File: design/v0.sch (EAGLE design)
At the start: 3 parts

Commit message: Update schematic
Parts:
- removed R1: 9.76k, rcl:R-EU_0207/10
- added D1, D2, D3, D4, D5, D6, D7, D8, D9: 1N4004, diode:1N4004
- added U$10, U$3, U$4, U$5, U$6, U$7, U$8, U$9: CHERRY-MX, cherrymx:CHERRY-MX
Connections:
- new net N$10: D1.C, D4.C, D7.C, U$1.24
- new net N$11: D2.C, D5.C, D8.C, U$1.22
- new net N$12: D3.C, D6.C, D9.C, U$1.21
- new net N$13: U$1.27, U$2.PIN-1, U$3.PIN-1, U$4.PIN-1
- new net N$14: U$1.26, U$5.PIN-1, U$6.PIN-1, U$7.PIN-1
- new net N$15: U$1.25, U$10.PIN-1, U$8.PIN-1, U$9.PIN-1
- new net N$3: D3.A, U$4.PIN-2
- new net N$5: D5.A, U$6.PIN-2
- new net N$6: D6.A, U$7.PIN-2
- new net N$7: D9.A, U$10.PIN-2
- new net N$8: D8.A, U$9.PIN-2
- new net N$9: D7.A, U$8.PIN-2
- net N$1: now also D1.A, U$2.PIN-2; no longer U$1.38, U$2.PIN-1
- net N$2: now also D2.A, U$3.PIN-2; no longer R1.2, U$1.36, U$2.PIN-2
- net N$4: now also D4.A, U$5.PIN-2; no longer R1.1, U$1.17
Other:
- moved on the sheet: U$2

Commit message: Update schematic
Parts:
- removed U$10, U$2, U$3, U$4, U$5, U$6, U$7, U$8, U$9: CHERRY-MX, cherrymx:CHERRY-MX
- added LED1, LED2, LED3: TLLG4400, led:TLLG4400
- added R1, R2: 9.76k, rcl:R-EU_VMTA55
- added R3, R4, R5: 60, rcl:R-EU_VMTA55
- added S1: RESET, switch-omron:10-XX
- added S2, S3: (no value), switch-omron:10-XX
- added U1, U2, U3, U4, U5, U6, U7, U8, U9: CHERRY-MX, cherrymx:CHERRY-MX
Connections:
- removed net N$15 (its old number): U$1.25, U$10.PIN-1, U$8.PIN-1, U$9.PIN-1
- removed net N$8: D8.A, U$9.PIN-2
- new net N$10: R1.1, R2.1, S2.S, S3.S, U$1.36
- new net N$11: R2.2, U$1.9
- new net N$12: S2.P, S3.P, U$1.8
- new net N$18: D6.A, U6.PIN-2
- new net N$19: D3.A, U3.PIN-2
- new net N$20: D9.A, U9.PIN-2
- new net N$21: D8.A, U8.PIN-2
- new net N$22: D5.A, U5.PIN-2
- new net N$23: D2.A, U2.PIN-2
- new net N$24: D1.A, U1.PIN-2
- new net N$25: D4.A, U4.PIN-2
- new net N$26: D7.A, U7.PIN-2
- new net N$27: U$1.27, U1.PIN-1, U2.PIN-1, U3.PIN-1
- new net N$28: U$1.26, U4.PIN-1, U5.PIN-1, U6.PIN-1
- new net N$29: U$1.25, U7.PIN-1, U8.PIN-1, U9.PIN-1
- net N$1: now also LED2.A, R4.1; no longer D1.A, U$2.PIN-2
- net N$13: now also S1.S, U$1.28; no longer U$1.27, U$2.PIN-1, U$3.PIN-1, U$4.PIN-1
- net N$14: now also S1.P, U$1.30; no longer U$1.26, U$5.PIN-1, U$6.PIN-1, U$7.PIN-1
- net N$2: now also LED1.A, R3.1; no longer D2.A, U$3.PIN-2
- net N$3: now also LED3.A, R5.1; no longer D3.A, U$4.PIN-2
- net N$4: now also LED1.C, LED2.C, LED3.C, U$1.3; no longer D4.A, U$5.PIN-2
- net N$5: now also R5.2, U$1.4; no longer D5.A, U$6.PIN-2
- net N$6: now also R4.2, U$1.5; no longer D6.A, U$7.PIN-2
- net N$7: now also R3.2, U$1.6; no longer D9.A, U$10.PIN-2
- net N$9: now also R1.2, U$1.7; no longer D7.A, U$8.PIN-2
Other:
- moved on the sheet: D1, D3, D4, D5, D6, D7, D8, D9

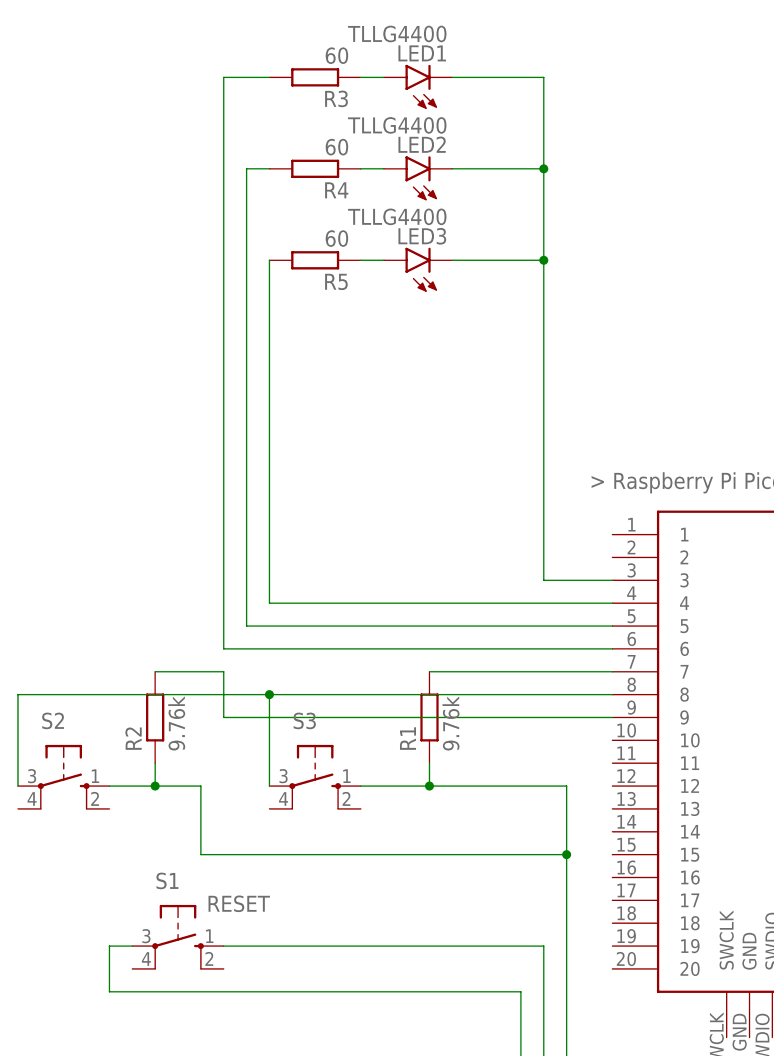
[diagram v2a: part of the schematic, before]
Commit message: Fix resistor locations on buttons
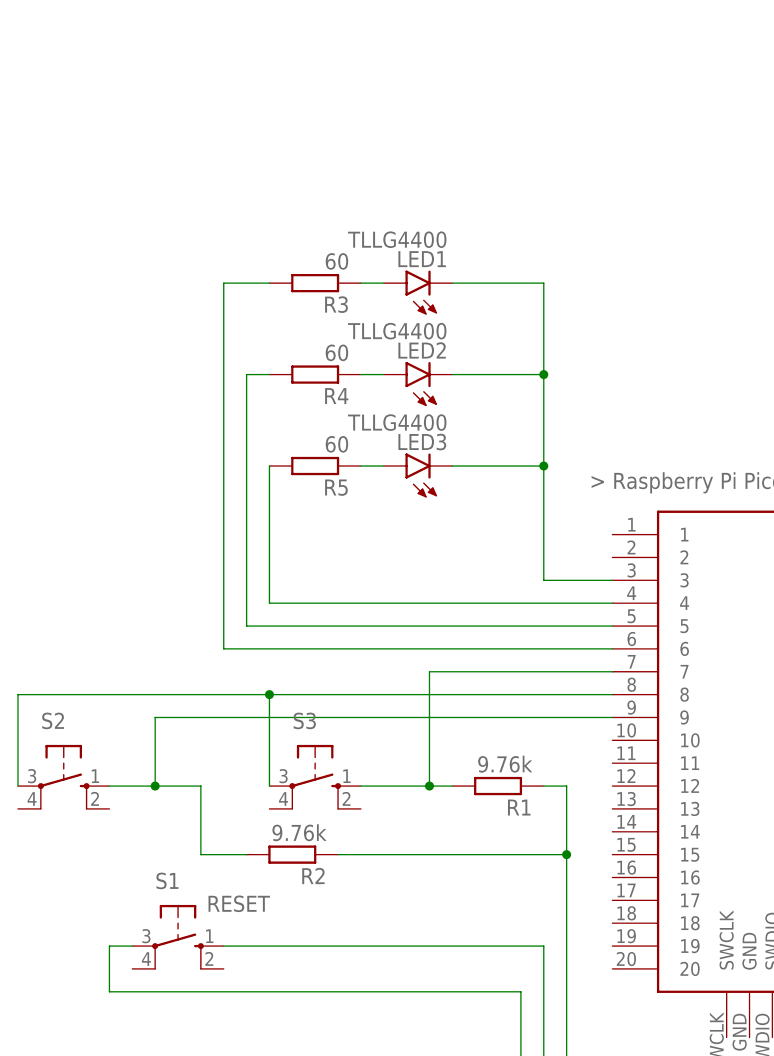
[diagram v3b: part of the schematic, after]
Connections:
- removed net N$9: R1.2, U$1.7
- new net N$8: R1.2, S3.S, U$1.7
- net N$10: no longer S2.S, S3.S
- net N$11: now also S2.S
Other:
- moved on the sheet: LED1, LED2, LED3, R1, R2, R3, R4, R5

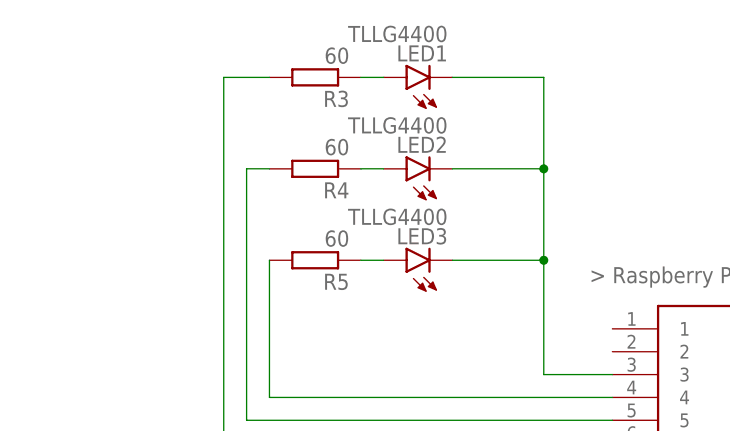
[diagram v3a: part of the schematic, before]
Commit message: Update LED resistor values
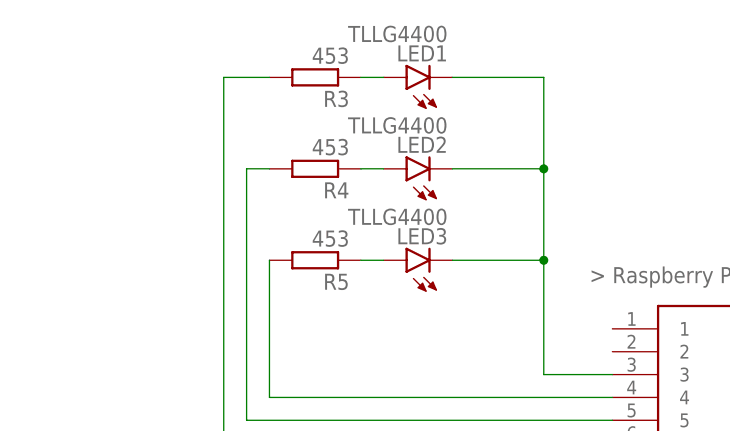
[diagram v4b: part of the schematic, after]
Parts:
- R3, R4, R5: value 60 -> 453
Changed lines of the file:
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@@
 <part name="LED2" library="led" library_urn="urn:adsk.eagle:library:259" deviceset="TLLG4400" device="" package3d_urn="urn:adsk.eagle:package:15797/1"/>
 <part name="LED3" library="led" library_urn="urn:adsk.eagle:library:259" deviceset="TLLG4400" device="" package3d_urn="urn:adsk.eagle:package:15797/1"/>
-<part name="R3" library="rcl" library_urn="urn:adsk.eagle:library:334" deviceset="R-EU_" device="VMTA55" package3d_urn="urn:adsk.eagle:package:26121/2" value="60"/>
-<part name="R4" library="rcl" library_urn="urn:adsk.eagle:library:334" deviceset="R-EU_" device="VMTA55" package3d_urn="urn:adsk.eagle:package:26121/2" value="60"/>
-<part name="R5" library="rcl" library_urn="urn:adsk.eagle:library:334" deviceset="R-EU_" device="VMTA55" package3d_urn="urn:adsk.eagle:package:26121/2" value="60"/>
+<part name="R3" library="rcl" library_urn="urn:adsk.eagle:library:334" deviceset="R-EU_" device="VMTA55" package3d_urn="urn:adsk.eagle:package:26121/2" value="453"/>
+<part name="R4" library="rcl" library_urn="urn:adsk.eagle:library:334" deviceset="R-EU_" device="VMTA55" package3d_urn="urn:adsk.eagle:package:26121/2" value="453"/>
+<part name="R5" library="rcl" library_urn="urn:adsk.eagle:library:334" deviceset="R-EU_" device="VMTA55" package3d_urn="urn:adsk.eagle:package:26121/2" value="453"/>
 </parts>
 <sheets>

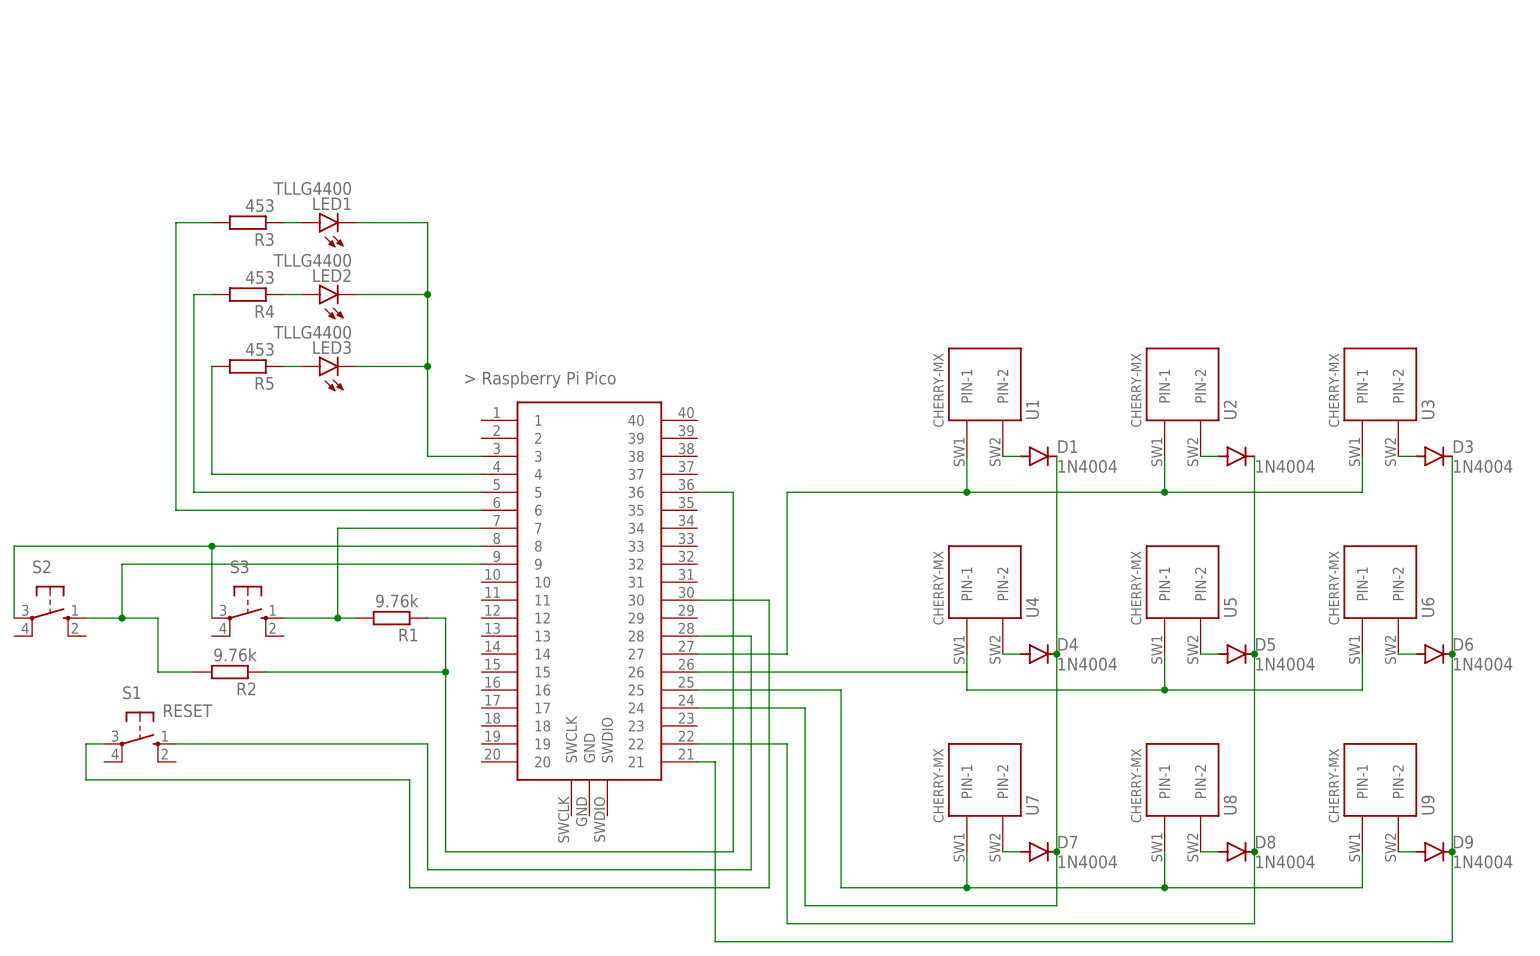
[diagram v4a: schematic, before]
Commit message: Switched component pins, added ground plane
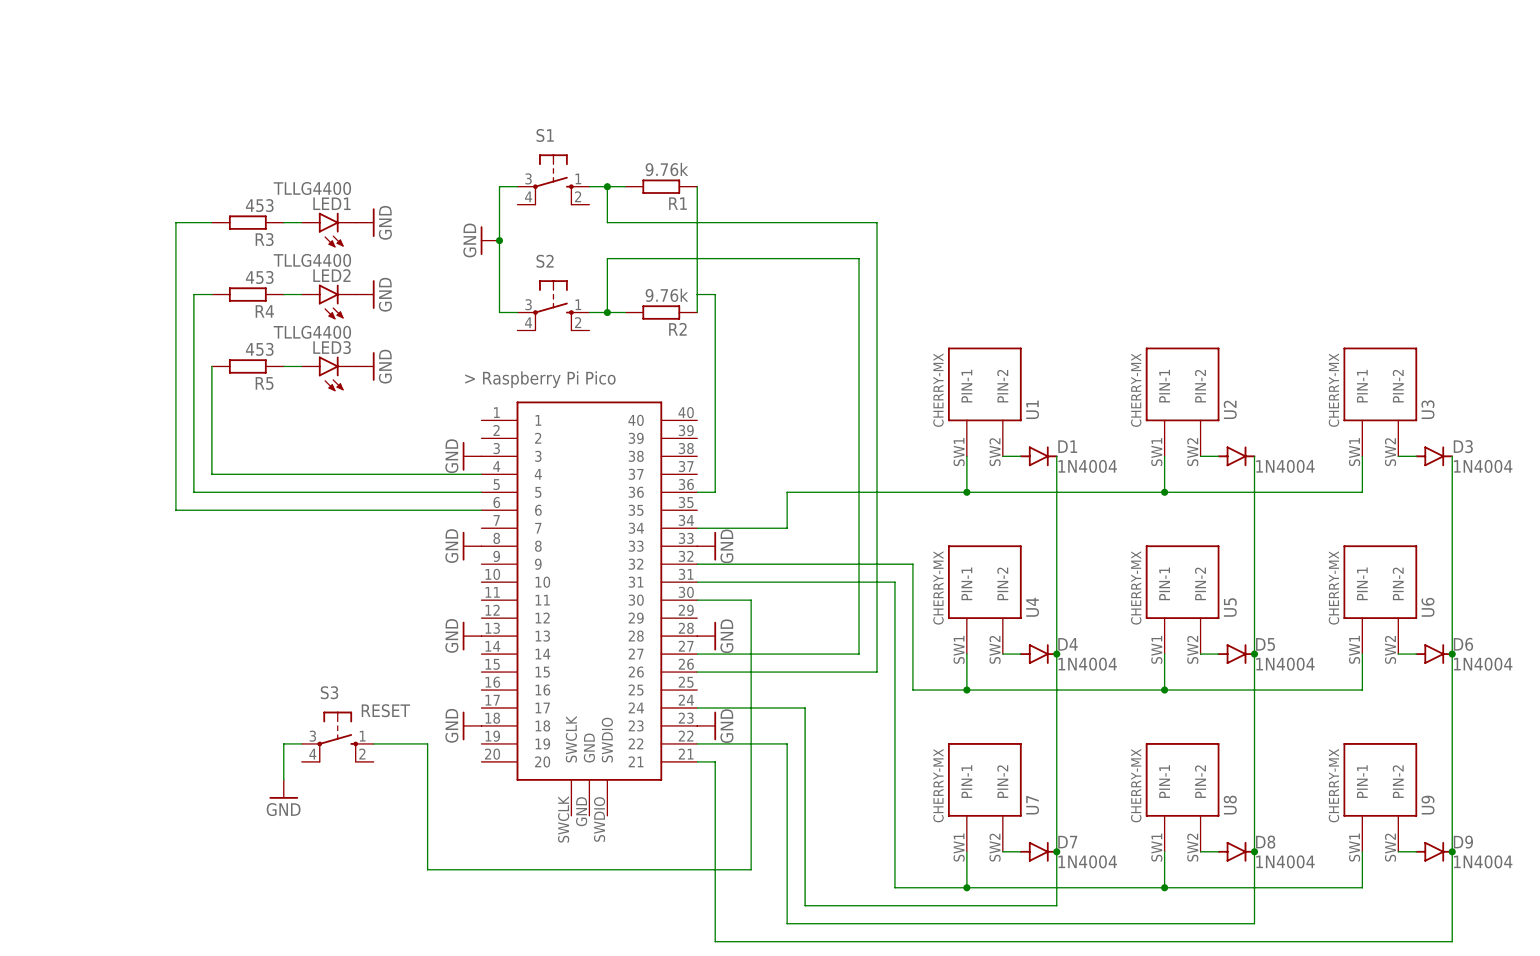
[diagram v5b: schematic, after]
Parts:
- S1: value RESET -> (none)
- S3: value (none) -> RESET
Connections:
- removed net N$11: R2.2, S2.S, U$1.9
- removed net N$12 (its old number): S2.P, S3.P, U$1.8
- removed net N$14: S1.P, U$1.30
- removed net N$8: R1.2, S3.S, U$1.7
- new net GND: LED1.C, LED2.C, LED3.C, S1.P, S2.P, S3.P, U$1.13, U$1.18, U$1.23, U$1.28, U$1.3, U$1.33, U$1.8
- new net N$9: R1.2, S1.S, U$1.26
- net N$13: now also S3.S, U$1.30; no longer S1.S, U$1.28
- net N$27: now also U$1.34; no longer U$1.27
- net N$28: now also U$1.32; no longer U$1.26
- net N$29: now also U$1.31; no longer U$1.25
- net N$4: now also R2.2, S2.S, U$1.27; no longer LED1.C, LED2.C, LED3.C, U$1.3
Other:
- moved on the sheet: R1, R2, S1, S2, S3

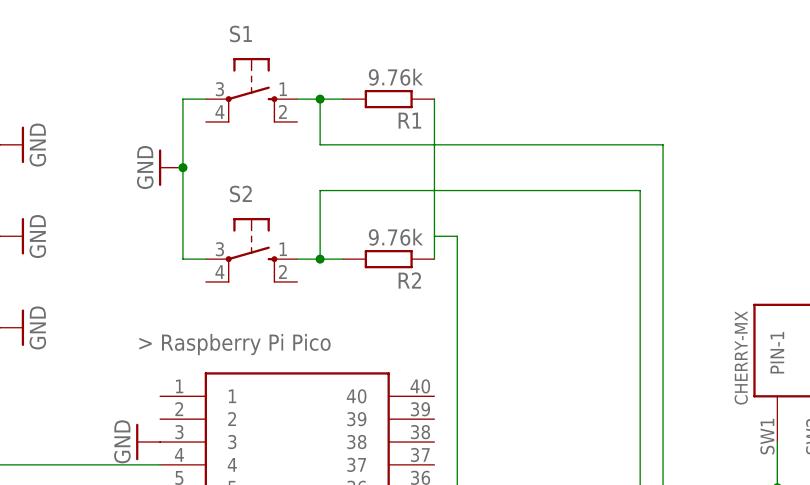
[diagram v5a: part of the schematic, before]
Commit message: Update net class width, swap R1/R2 names
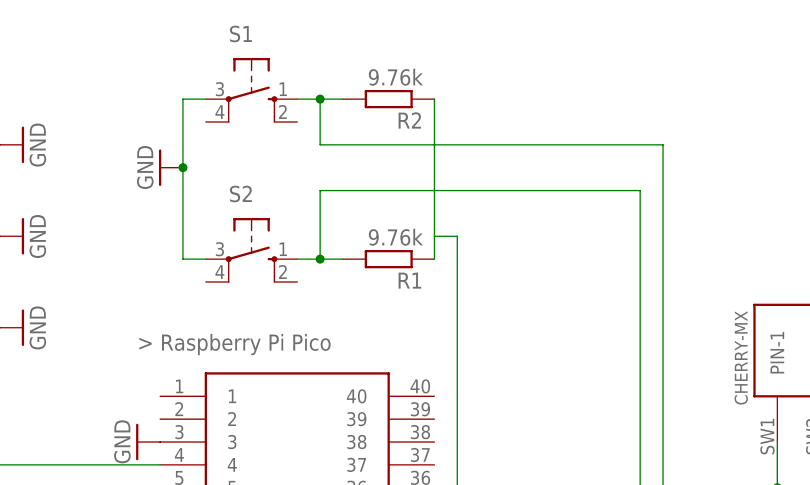
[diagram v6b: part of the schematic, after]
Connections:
- net N$4: now also R1.2; no longer R2.2
- net N$9: now also R2.2; no longer R1.2
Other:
- moved on the sheet: R1, R2
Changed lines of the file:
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@@
 </variantdefs>
 <classes>
-<class number="0" name="default" width="0" drill="0">
+<class number="0" name="default" width="0.3048" drill="0">
 </class>
 </classes>
@@
 <part name="GND11" library="supply1" library_urn="urn:adsk.eagle:library:371" deviceset="GND" device=""/>
 <part name="S2" library="switch-omron" library_urn="urn:adsk.eagle:library:377" deviceset="10-XX" device="" package3d_urn="urn:adsk.eagle:package:27496/1"/>
+<part name="R1" library="rcl" library_urn="urn:adsk.eagle:library:334" deviceset="R-EU_" device="VMTA55" package3d_urn="urn:adsk.eagle:package:26121/2" value="9.76k"/>
+<part name="S1" library="switch-omron" library_urn="urn:adsk.eagle:library:377" deviceset="10-XX" device="" package3d_urn="urn:adsk.eagle:package:27496/1"/>
 <part name="R2" library="rcl" library_urn="urn:adsk.eagle:library:334" deviceset="R-EU_" device="VMTA55" package3d_urn="urn:adsk.eagle:package:26121/2" value="9.76k"/>
-<part name="S1" library="switch-omron" library_urn="urn:adsk.eagle:library:377" deviceset="10-XX" device="" package3d_urn="urn:adsk.eagle:package:27496/1"/>
-<part name="R1" library="rcl" library_urn="urn:adsk.eagle:library:334" deviceset="R-EU_" device="VMTA55" package3d_urn="urn:adsk.eagle:package:26121/2" value="9.76k"/>
 <part name="GND13" library="supply1" library_urn="urn:adsk.eagle:library:371" deviceset="GND" device=""/>
 </parts>
@@
 <attribute name="VALUE" x="79.375" y="87.63" size="1.778" layer="96"/>
 </instance>
-<instance part="R2" gate="G$1" x="91.44" y="83.82" smashed="yes" rot="R180">
+<instance part="R1" gate="G$1" x="91.44" y="83.82" smashed="yes" rot="R180">
 <attribute name="NAME" x="95.25" y="82.3214" size="1.778" layer="95" rot="R180"/>
 <attribute name="VALUE" x="95.25" y="87.122" size="1.778" layer="96" rot="R180"/>
@@
 <attribute name="VALUE" x="79.375" y="105.41" size="1.778" layer="96"/>
 </instance>
-<instance part="R1" gate="G$1" x="91.44" y="101.6" smashed="yes" rot="R180">
+<instance part="R2" gate="G$1" x="91.44" y="101.6" smashed="yes" rot="R180">
 <attribute name="NAME" x="95.25" y="100.1014" size="1.778" layer="95" rot="R180"/>
 <attribute name="VALUE" x="95.25" y="104.902" size="1.778" layer="96" rot="R180"/>
@@
 <segment>
 <pinref part="S2" gate="1" pin="S"/>
-<pinref part="R2" gate="G$1" pin="2"/>
+<pinref part="R1" gate="G$1" pin="2"/>
 <wire x1="81.28" y1="83.82" x2="83.82" y2="83.82" width="0.1524" layer="91"/>
 <wire x1="83.82" y1="83.82" x2="86.36" y2="83.82" width="0.1524" layer="91"/>
@@
 <segment>
 <pinref part="S1" gate="1" pin="S"/>
-<pinref part="R1" gate="G$1" pin="2"/>
+<pinref part="R2" gate="G$1" pin="2"/>
 <wire x1="81.28" y1="101.6" x2="83.82" y2="101.6" width="0.1524" layer="91"/>
 <wire x1="83.82" y1="101.6" x2="86.36" y2="101.6" width="0.1524" layer="91"/>
@@
 <net name="N$12" class="0">
 <segment>
+<pinref part="R2" gate="G$1" pin="1"/>
 <pinref part="R1" gate="G$1" pin="1"/>
-<pinref part="R2" gate="G$1" pin="1"/>
 <wire x1="96.52" y1="101.6" x2="96.52" y2="86.36" width="0.1524" layer="91"/>
 <wire x1="96.52" y1="86.36" x2="96.52" y2="83.82" width="0.1524" layer="91"/>
